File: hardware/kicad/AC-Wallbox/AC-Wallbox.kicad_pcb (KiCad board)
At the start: 4 copper layers, 150 x 100 mm, 0 parts

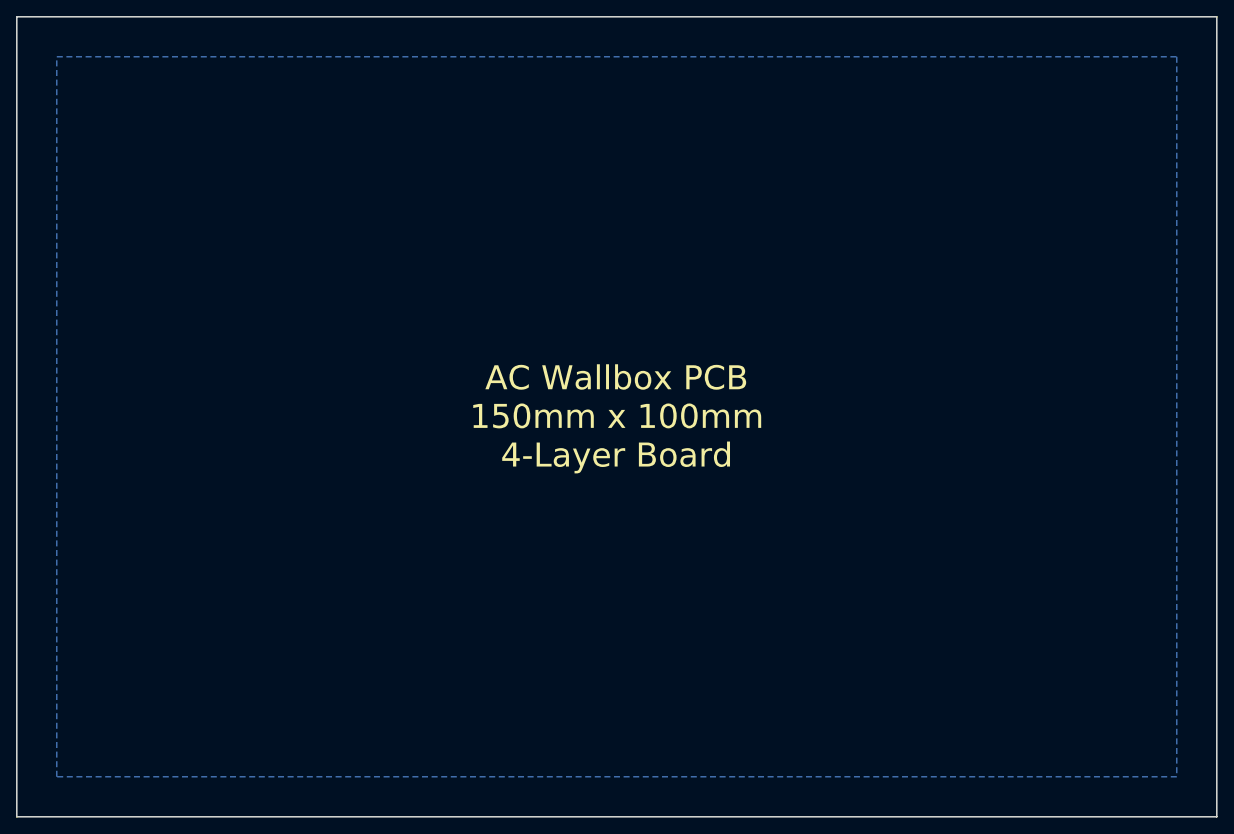
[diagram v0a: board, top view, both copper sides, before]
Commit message: اصلاح syntax فایل‌های PCB برای سازگاری با KiCad
- اصلاح فرمت DC-FastCharger.kicad_pcb
- اصلاح فرمت AC-Wallbox.kicad_pcb
- رفع خطای 'Expecting left, right, top, bottom, or mirror'
- استفاده از syntax صحیح KiCad version 20221018
- افزودن tstamp های صحیح
- فایل‌ها اکنون بدون خطا در KiCad باز می‌شوند
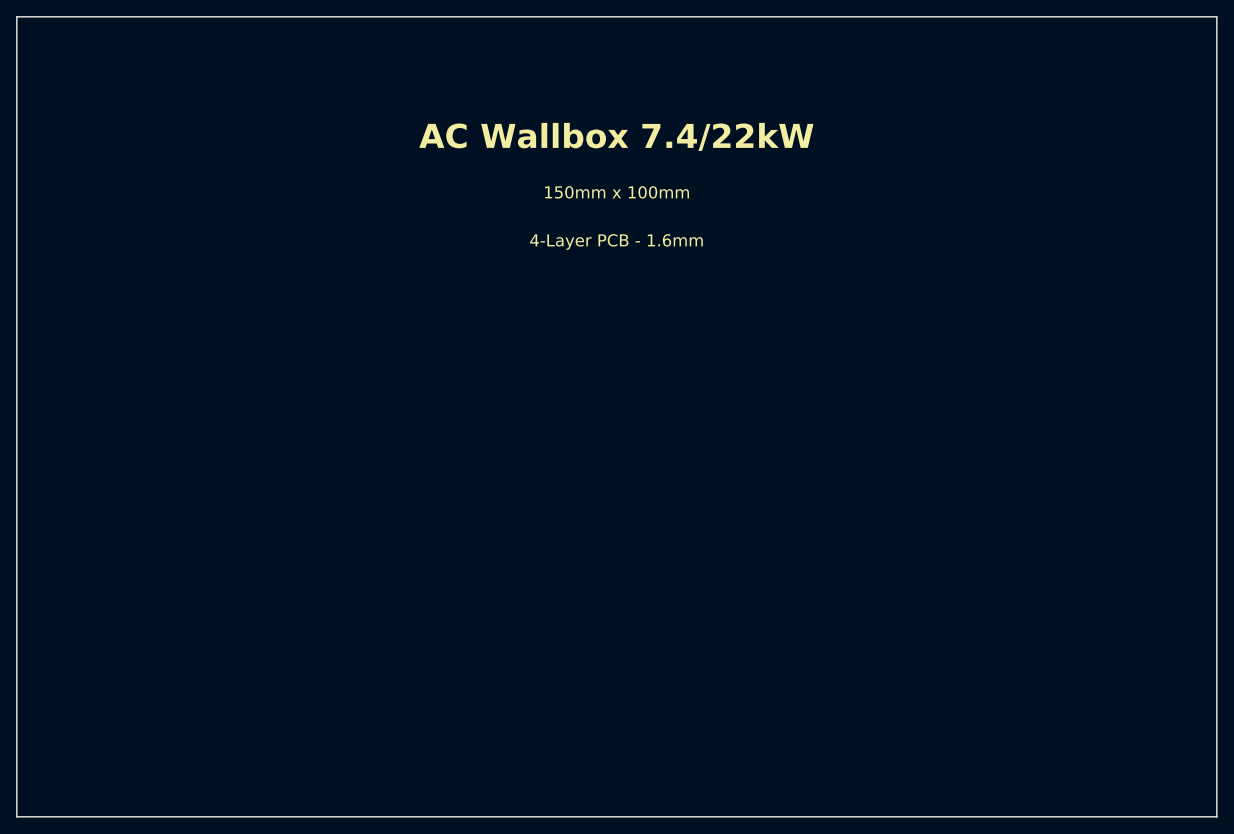
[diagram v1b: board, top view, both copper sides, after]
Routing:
- added copper zone on In2.Cu, net +12V
- added copper zone on In1.Cu, net GND
- removed copper zone on In1.Cu, net +12V
- removed copper zone on B.Cu, net GND
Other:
- board text added: "150mm x 100mm"
- board text added: "4-Layer PCB - 1.6mm"
- board text added: "AC Wallbox 7.4/22kW"
- board text removed: "AC Wallbox PCB 150mm x 100mm 4-Layer Board"
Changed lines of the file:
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@@
   (general
     (thickness 1.6)
+    (legacy_teardrops no)
   )
   (paper "A3")
@@
     (40 "Dwgs.User" user "User.Drawings")
     (41 "Cmts.User" user "User.Comments")
-    (42 "Eco1.User" user "User.Eco1")
-    (43 "Eco2.User" user "User.Eco2")
     (44 "Edge.Cuts" user)
     (45 "Margin" user)
@@
   (setup
     (pad_to_mask_clearance 0)
+    (grid_origin 0 0)
     (pcbplotparams
       (layerselection 0x00010fc_ffffffff)
       (plot_on_all_layers_selection 0x0000000_00000000)
-      (disableapertmacros false)
-      (usegerberextensions false)
-      (usegerberattributes true)
-      (usegerberadvancedattributes true)
-      (creategerberjobfile true)
+      (disableapertmacros no)
+      (usegerberextensions no)
+      (usegerberattributes yes)
+      (usegerberadvancedattributes yes)
+      (creategerberjobfile yes)
       (dashed_line_dash_ratio 12.000000)
       (dashed_line_gap_ratio 3.000000)
       (svgprecision 4)
-      (plotframeref false)
-      (viasonmask false)
+      (plotframeref no)
+      (viasonmask no)
       (mode 1)
-      (useauxorigin false)
+      (useauxorigin no)
       (hpglpennumber 1)
       (hpglpenspeed 20)
       (hpglpendiameter 15.000000)
-      (dxfpolygonmode true)
-      (dxfimperialunits true)
-      (dxfusepcbnewfont true)
-      (psnegative false)
-      (psa4output false)
-      (plotreference true)
-      (plotvalue true)
-      (plotinvisibletext false)
-      (sketchpadsonfab false)
-      (subtractmaskfromsilk false)
+      (pdf_front_fp_property_popups yes)
+      (pdf_back_fp_property_popups yes)
+      (dxfpolygonmode yes)
+      (dxfimperialunits yes)
+      (dxfusepcbnewfont yes)
+      (psnegative no)
+      (psa4output no)
+      (plotreference yes)
+      (plotvalue yes)
+      (plotfptext yes)
+      (plotinvisibletext no)
+      (sketchpadsonfab no)
+      (subtractmaskfromsilk no)
       (outputformat 1)
-      (mirror false)
+      (mirror no)
       (drillshape 0)
       (scaleselection 1)
-      (outputdirectory "gerber/")
+      (outputdirectory "")
     )
   )
@@
   (net 3 "+5V")
   (net 4 "+3.3V")
-  (net 5 "-12V")
-  (net 6 "AC_L")
-  (net 7 "AC_N")
-  (net 8 "PE")
-  (net 9 "CP_OUT")
-  (net 10 "PP_SENSE")
-  (gr_rect (start 10 10) (end 160 110)
-    (stroke (width 0.2) (type solid)) (fill none) (layer "Edge.Cuts") (tstamp edge-cut-1))
-  (gr_text "AC Wallbox PCB\n150mm x 100mm\n4-Layer Board" (at 85 60 0) (layer "F.SilkS") (tstamp text-board-info)
-    (effects (font (size 3 3) (thickness 0.5)) (justify center))
+  (gr_line (start 10 10) (end 160 10)
+    (stroke (width 0.2) (type solid)) (layer "Edge.Cuts"))
+  (gr_line (start 160 10) (end 160 110)
+    (stroke (width 0.2) (type solid)) (layer "Edge.Cuts"))
+  (gr_line (start 160 110) (end 10 110)
+    (stroke (width 0.2) (type solid)) (layer "Edge.Cuts"))
+  (gr_line (start 10 110) (end 10 10)
+    (stroke (width 0.2) (type solid)) (layer "Edge.Cuts"))
+  (gr_text "AC Wallbox 7.4/22kW" (at 85 25 0) (layer "F.SilkS")
+    (effects (font (size 3 3) (thickness 0.5) bold) (justify center))
   )
-  (gr_text "POWER SECTION" (at 40 30 0) (layer "Cmts.User") (tstamp text-power)
+  (gr_text "150mm x 100mm" (at 85 32 0) (layer "F.SilkS")
+    (effects (font (size 1.5 1.5) (thickness 0.25)) (justify center))
+  )
+  (gr_text "4-Layer PCB - 1.6mm" (at 85 38 0) (layer "F.SilkS")
+    (effects (font (size 1.5 1.5) (thickness 0.25)) (justify center))
+  )
+  (gr_line (start 80 45) (end 80 105)
+    (stroke (width 0.3) (type dash)) (layer "Cmts.User"))
+  (gr_text "POWER SECTION" (at 40 50 0) (layer "Cmts.User")
     (effects (font (size 2 2) (thickness 0.3)) (justify center))
   )
-  (gr_text "CONTROL SECTION" (at 120 30 0) (layer "Cmts.User") (tstamp text-control)
+  (gr_text "CONTROL SECTION" (at 120 50 0) (layer "Cmts.User")
     (effects (font (size 2 2) (thickness 0.3)) (justify center))
   )
-  (gr_line (start 80 20) (end 80 100)
-    (stroke (width 0.5) (type dash)) (layer "Cmts.User") (tstamp line-separation))
-  (zone (net 1) (net_name "GND") (layer "F.Cu") (tstamp zone-gnd-f)
-    (hatch edge 0.508)
+  (zone (net 1) (net_name "GND") (layer "In1.Cu") (hatch edge 0.5)
     (connect_pads (clearance 0.2))
-    (min_thickness 0.2)
-    (filled_areas_thickness no)
-    (keepout (tracks not_allowed) (vias not_allowed) (pads not_allowed) (copperpour not_allowed) (footprints not_allowed))
-    (fill yes (thermal_gap 0.508) (thermal_bridge_width 0.508))
+    (min_thickness 0.2) (filled_areas_thickness no)
+    (fill yes (thermal_gap 0.5) (thermal_bridge_width 0.5))
     (polygon
       (pts
@@
     )
   )
-  (zone (net 1) (net_name "GND") (layer "B.Cu") (tstamp zone-gnd-b)
-    (hatch edge 0.508)
-    (connect_pads (clearance 0.2))
-    (min_thickness 0.2)
-    (filled_areas_thickness no)
-    (fill yes (thermal_gap 0.508) (thermal_bridge_width 0.508))
-    (polygon
-      (pts
-        (xy 15 15)
-        (xy 155 15)
-        (xy 155 105)
-        (xy 15 105)
-      )
-    )
-  )
-  (zone (net 2) (net_name "+12V") (layer "In1.Cu") (tstamp zone-12v)
-    (hatch edge 0.508)
+  (zone (net 2) (net_name "+12V") (layer "In2.Cu") (hatch edge 0.5)
     (connect_pads (clearance 0.3))
-    (min_thickness 0.3)
-    (fill yes (thermal_gap 0.508) (thermal_bridge_width 0.508))
+    (min_thickness 0.3) (filled_areas_thickness no)
+    (fill yes (thermal_gap 0.5) (thermal_bridge_width 0.5))
     (polygon
       (pts
@@
     )
   )
-  (zone (net 4) (net_name "+3.3V") (layer "In2.Cu") (tstamp zone-3v3)
-    (hatch edge 0.508)
+  (zone (net 4) (net_name "+3.3V") (layer "In2.Cu") (hatch edge 0.5)
     (connect_pads (clearance 0.2))
-    (min_thickness 0.2)
-    (fill yes (thermal_gap 0.508) (thermal_bridge_width 0.508))
+    (min_thickness 0.2) (filled_areas_thickness no)
+    (fill yes (thermal_gap 0.5) (thermal_bridge_width 0.5))
     (polygon
       (pts
